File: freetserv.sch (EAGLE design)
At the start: 63 parts, among them IC2 SN75240PW, Q1 12MHz, Q2 6MHz, U1 MCP16311-E/MS, U4 TLV810SDBZT, U5 SN74LVC1G86DCKR

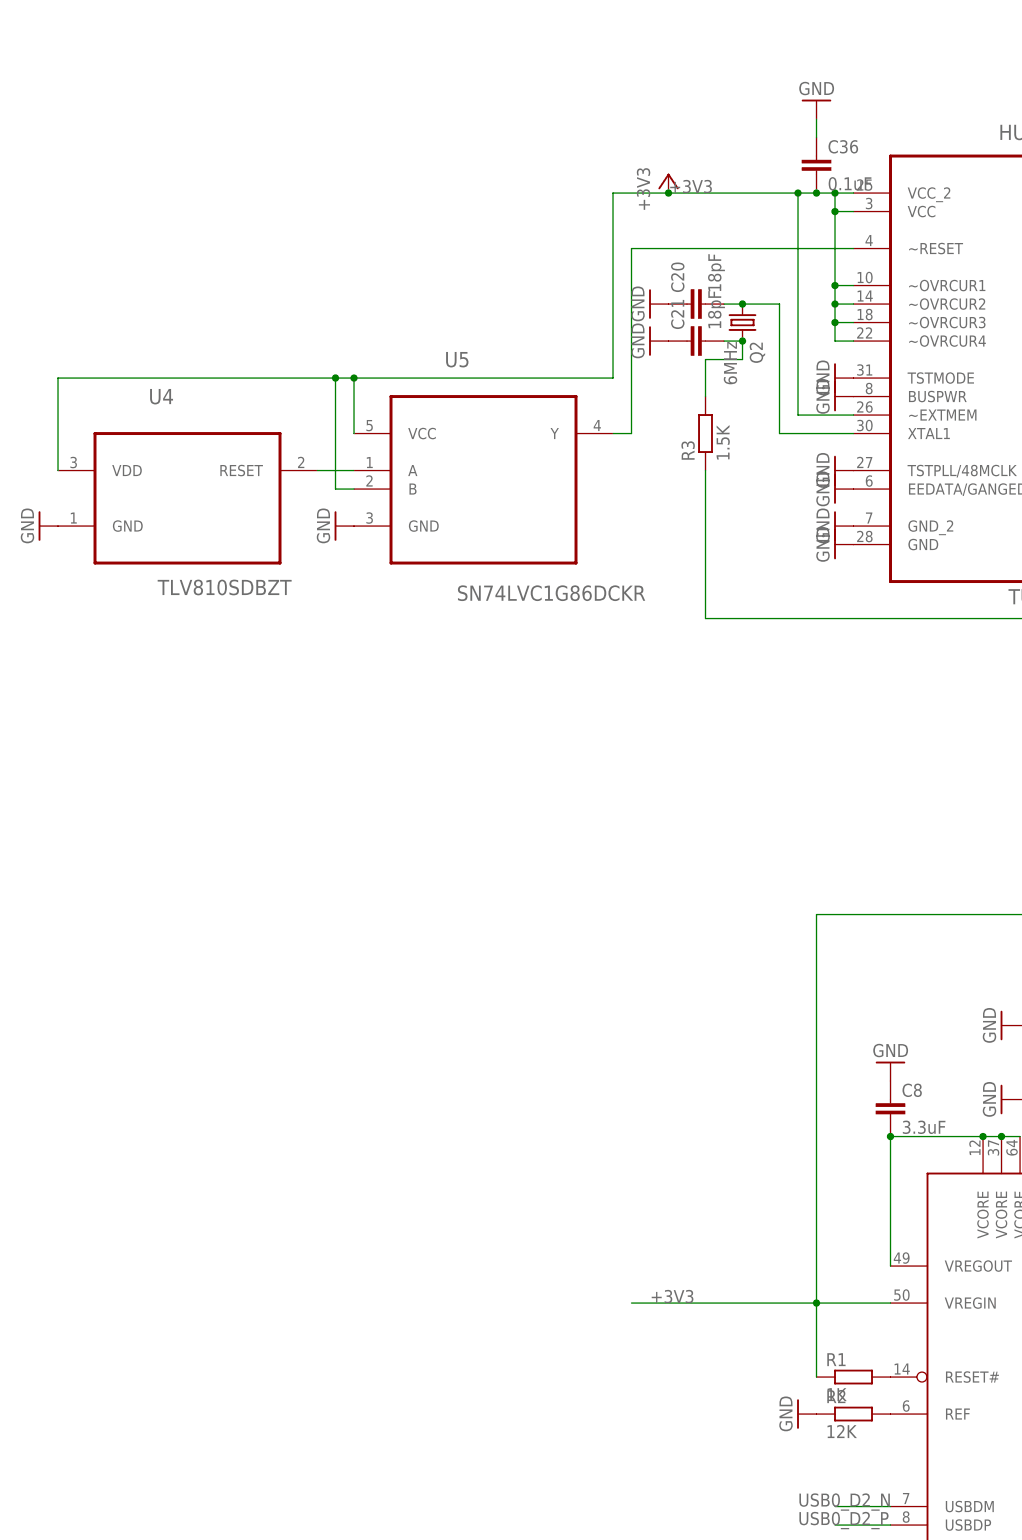
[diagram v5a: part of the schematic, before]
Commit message: replace volt supervisor IC with R/C circuit
Not yet routed to the FTDI, because that area still needs some
re-routing anyway.

fixes #5
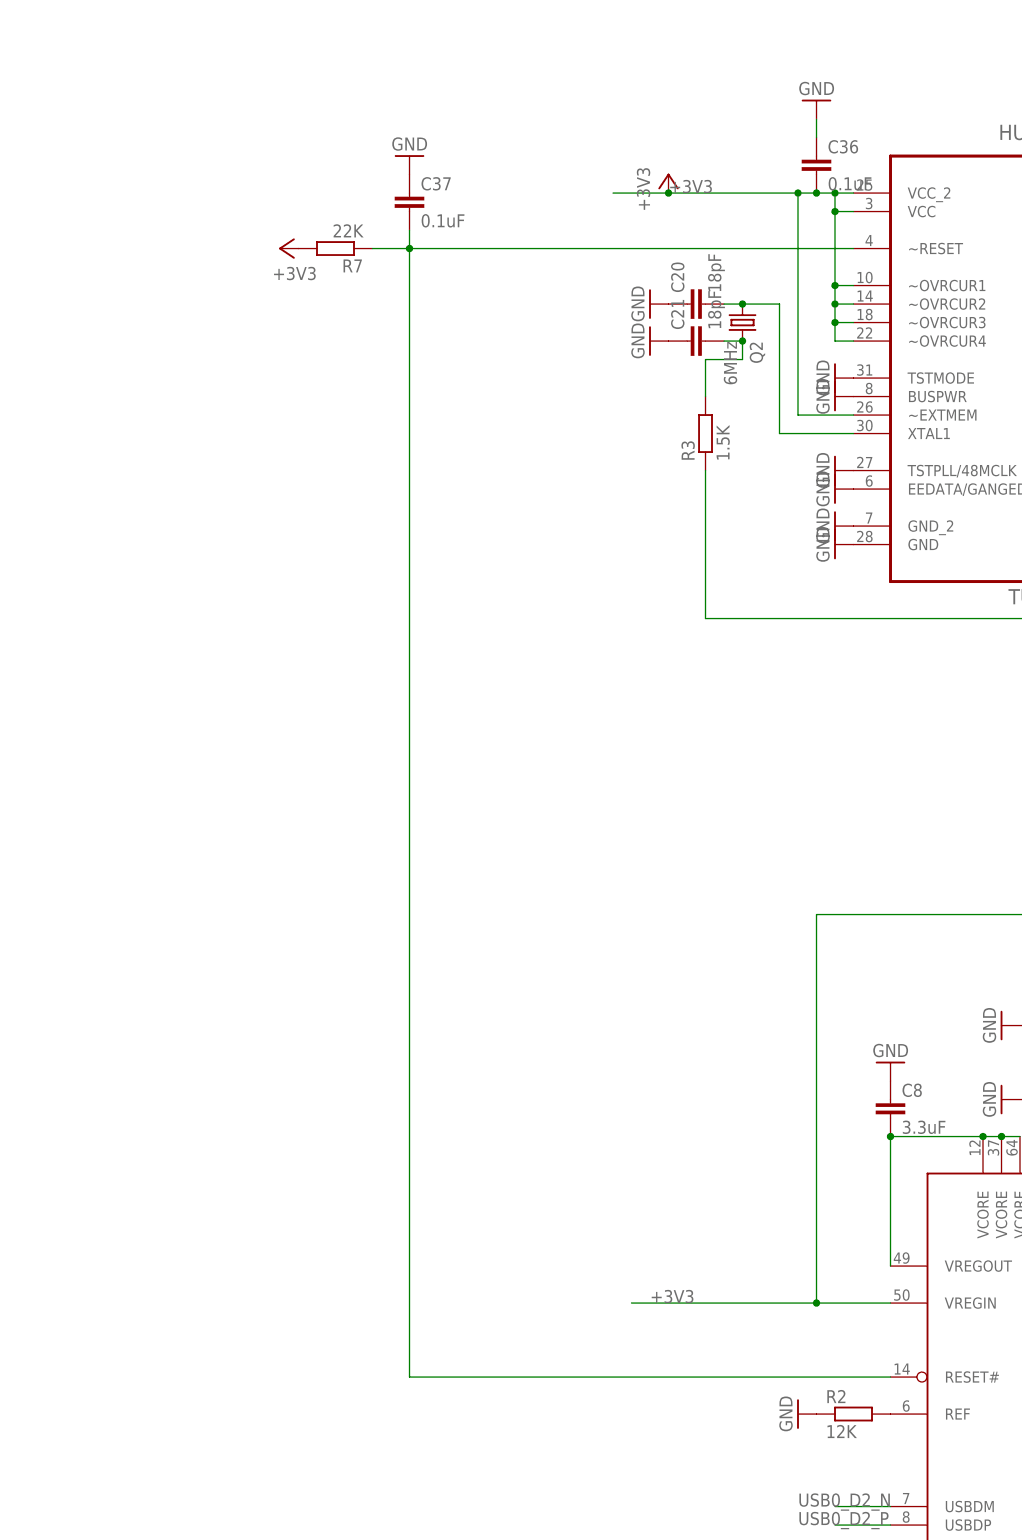
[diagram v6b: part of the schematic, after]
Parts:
- removed R1: 1K, resistor:R-EU_R0805
- removed U4: TLV810SDBZT, Texas Instruments_By_element14_Batch_1:TLV810SDBZT
- removed U5: SN74LVC1G86DCKR, Texas Instruments_By_element14_Batch_1:SN74LVC1G86DCKR
- added C37: 0.1uF, resistor:C-EUC0805
- added R7: 22K, resistor:R-EU_R0805
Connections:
- removed net N$13: R1.2, SERIAL0CORE.RESET#
- removed net N$42: U4.RESET, U5.A
- net +3V3: now also R7.2; no longer R1.1, U4.VDD, U5.B, U5.VCC
- net GND: now also C37.1; no longer U4.GND, U5.GND
- net N$43: now also C37.2, R7.1, SERIAL0CORE.RESET#; no longer U5.Y
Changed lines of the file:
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@@
 </part>
 <part name="GND14" library="supply1" deviceset="GND" device=""/>
-<part name="R1" library="resistor" deviceset="R-EU_" device="R0805" value="1K">
-<attribute name="PARTNO" value="311-1.0KARCT-ND"/>
-</part>
 <part name="R2" library="resistor" deviceset="R-EU_" device="R0805" value="12K">
 <attribute name="PARTNO" value="311-12.0KCRCT-ND"/>
@@
 <part name="GND23" library="supply1" deviceset="GND" device=""/>
 <part name="GND24" library="supply1" deviceset="GND" device=""/>
-<part name="U4" library="Texas Instruments_By_element14_Batch_1" deviceset="TLV810SDBZT" device=""/>
 <part name="DRIVER0A" library="Texas Instruments_By_element14_Batch_1" deviceset="MAX3232CPWR" device="">
 <attribute name="PARTNO" value="296-19263-1-ND"/>
@@
 <part name="GND28" library="supply1" deviceset="GND" device=""/>
 <part name="GND29" library="supply1" deviceset="GND" device=""/>
-<part name="GND30" library="supply1" deviceset="GND" device=""/>
 <part name="C19" library="resistor" deviceset="C-EU" device="C0805" value="0.1uF">
 <attribute name="PARTNO" value="1276-1003-1-ND"/>
 </part>
 <part name="GND31" library="supply1" deviceset="GND" device=""/>
-<part name="U5" library="Texas Instruments_By_element14_Batch_1" deviceset="SN74LVC1G86DCKR" device=""/>
-<part name="GND32" library="supply1" deviceset="GND" device=""/>
 <part name="Q2" library="crystal" deviceset="CSM-7X-DU" device="" value="6MHz">
 <attribute name="PARTNO" value="535-10208-1-ND"/>
@@
 </part>
 <part name="P+2" library="supply1" deviceset="+3V3" device=""/>
+<part name="C37" library="resistor" deviceset="C-EU" device="C0805" value="0.1uF">
+<attribute name="PARTNO" value="1276-1003-1-ND"/>
+</part>
+<part name="R7" library="resistor" deviceset="R-EU_" device="R0805" value="22K">
+<attribute name="PARTNO" value="311-22KARCT-ND"/>
+</part>
+<part name="P+3" library="supply1" deviceset="+3V3" device=""/>
+<part name="GND30" library="supply1" deviceset="GND" device=""/>
 </parts>
 <sheets>
@@
 </instance>
 <instance part="GND14" gate="1" x="5.08" y="104.14" rot="R180"/>
-<instance part="R1" gate="G$1" x="0" y="60.96">
-<attribute name="PARTNO" x="0" y="60.96" size="1.778" layer="96" display="off"/>
-</instance>
 <instance part="R2" gate="G$1" x="0" y="55.88">
 <attribute name="PARTNO" x="0" y="55.88" size="1.778" layer="96" display="off"/>
@@
 <instance part="GND23" gate="1" x="45.72" y="109.22" rot="R90"/>
 <instance part="GND24" gate="1" x="45.72" y="99.06" rot="R90"/>
-<instance part="U4" gate="A" x="-91.44" y="185.42"/>
 <instance part="DRIVER0A" gate="A" x="160.02" y="99.06">
 <attribute name="PARTNO" x="160.02" y="99.06" size="1.778" layer="96" display="off"/>
@@
 <instance part="GND28" gate="1" x="132.08" y="78.74" rot="R270"/>
 <instance part="GND29" gate="1" x="132.08" y="114.3" rot="R270"/>
-<instance part="GND30" gate="1" x="-111.76" y="177.8" rot="R270"/>
 <instance part="C19" gate="G$1" x="127" y="111.76" rot="R180">
 <attribute name="PARTNO" x="127" y="111.76" size="1.778" layer="96" display="off"/>
 </instance>
 <instance part="GND31" gate="1" x="127" y="106.68"/>
-<instance part="U5" gate="A" x="-50.8" y="187.96"/>
-<instance part="GND32" gate="1" x="-71.12" y="177.8" rot="R270"/>
 <instance part="Q2" gate="P" x="-15.24" y="205.74" rot="R270">
 <attribute name="PARTNO" x="-15.24" y="205.74" size="1.778" layer="96" display="off"/>
@@
 </instance>
 <instance part="P+2" gate="G$1" x="-25.4" y="226.06"/>
+<instance part="C37" gate="G$1" x="-60.96" y="223.52">
+<attribute name="PARTNO" x="-60.96" y="223.52" size="1.778" layer="96" display="off"/>
+</instance>
+<instance part="R7" gate="G$1" x="-71.12" y="215.9" rot="R180">
+<attribute name="PARTNO" x="-71.12" y="215.9" size="1.778" layer="96" rot="R90" display="off"/>
+</instance>
+<instance part="P+3" gate="G$1" x="-78.74" y="215.9" rot="R90"/>
+<instance part="GND30" gate="1" x="-60.96" y="228.6" rot="R180"/>
 </instances>
 <busses>
@@
 </segment>
 <segment>
-<pinref part="U4" gate="A" pin="GND"/>
-<pinref part="GND30" gate="1" pin="GND"/>
-</segment>
-<segment>
 <pinref part="C19" gate="G$1" pin="1"/>
 <pinref part="GND31" gate="1" pin="GND"/>
-</segment>
-<segment>
-<pinref part="U5" gate="A" pin="GND"/>
-<pinref part="GND32" gate="1" pin="GND"/>
 </segment>
 <segment>
@@
 <pinref part="GND49" gate="1" pin="GND"/>
 </segment>
+<segment>
+<pinref part="C37" gate="G$1" pin="1"/>
+<pinref part="GND30" gate="1" pin="GND"/>
+</segment>
 </net>
 <net name="USB0_DM_P" class="0">
@@
 </segment>
 </net>
-<net name="N$13" class="0">
-<segment>
-<pinref part="SERIAL0" gate="CORE" pin="RESET#"/>
-<pinref part="R1" gate="G$1" pin="2"/>
-</segment>
-</net>
 <net name="N$14" class="0">
 <segment>
@@
 </segment>
 </net>
-<net name="N$42" class="0">
-<segment>
-<pinref part="U4" gate="A" pin="RESET"/>
-<pinref part="U5" gate="A" pin="A"/>
-<wire x1="-73.66" y1="185.42" x2="-68.58" y2="185.42" width="0.1524" layer="91"/>
-</segment>
-</net>
 <net name="N$43" class="0">
 <segment>
 <pinref part="HUB0" gate="A" pin="~RESET"/>
-<wire x1="0" y1="215.9" x2="-30.48" y2="215.9" width="0.1524" layer="91"/>
-<pinref part="U5" gate="A" pin="Y"/>
-<wire x1="-30.48" y1="190.5" x2="-33.02" y2="190.5" width="0.1524" layer="91"/>
-<wire x1="-30.48" y1="215.9" x2="-30.48" y2="190.5" width="0.1524" layer="91"/>
+<pinref part="R7" gate="G$1" pin="1"/>
+<wire x1="-66.04" y1="215.9" x2="-60.96" y2="215.9" width="0.1524" layer="91"/>
+<pinref part="C37" gate="G$1" pin="2"/>
+<wire x1="-60.96" y1="215.9" x2="0" y2="215.9" width="0.1524" layer="91"/>
+<wire x1="-60.96" y1="218.44" x2="-60.96" y2="215.9" width="0.1524" layer="91"/>
+<junction x="-60.96" y="215.9"/>
+<pinref part="SERIAL0" gate="CORE" pin="RESET#"/>
+<wire x1="5.08" y1="60.96" x2="-60.96" y2="60.96" width="0.1524" layer="91"/>
+<wire x1="-60.96" y1="60.96" x2="-60.96" y2="215.9" width="0.1524" layer="91"/>
 </segment>
 </net>
@@
 <net name="+3V3" class="2">
 <segment>
-<pinref part="U4" gate="A" pin="VDD"/>
-<wire x1="-109.22" y1="185.42" x2="-109.22" y2="198.12" width="0.1524" layer="91"/>
-<wire x1="-109.22" y1="198.12" x2="-71.12" y2="198.12" width="0.1524" layer="91"/>
-<wire x1="-71.12" y1="198.12" x2="-68.58" y2="198.12" width="0.1524" layer="91"/>
-<wire x1="-68.58" y1="198.12" x2="-33.02" y2="198.12" width="0.1524" layer="91"/>
-<pinref part="U5" gate="A" pin="VCC"/>
-<wire x1="-68.58" y1="190.5" x2="-68.58" y2="198.12" width="0.1524" layer="91"/>
-<junction x="-68.58" y="198.12"/>
-<pinref part="U5" gate="A" pin="B"/>
-<wire x1="-68.58" y1="182.88" x2="-71.12" y2="182.88" width="0.1524" layer="91"/>
-<wire x1="-71.12" y1="182.88" x2="-71.12" y2="198.12" width="0.1524" layer="91"/>
-<junction x="-71.12" y="198.12"/>
 <pinref part="HUB0" gate="A" pin="VCC_2"/>
 <wire x1="-7.62" y1="223.52" x2="-5.08" y2="223.52" width="0.1524" layer="91"/>
@@
 <label x="-25.4" y="223.52" size="1.778" layer="95"/>
 <wire x1="-25.4" y1="223.52" x2="-7.62" y2="223.52" width="0.1524" layer="91"/>
-<wire x1="-33.02" y1="223.52" x2="-33.02" y2="198.12" width="0.1524" layer="91"/>
 <pinref part="C36" gate="G$1" pin="2"/>
 <junction x="-5.08" y="223.52"/>
@@
 <pinref part="SERIAL0" gate="CORE" pin="VREGIN"/>
 <wire x1="-30.48" y1="71.12" x2="-5.08" y2="71.12" width="0.1524" layer="91"/>
-<pinref part="R1" gate="G$1" pin="1"/>
 <wire x1="-5.08" y1="71.12" x2="5.08" y2="71.12" width="0.1524" layer="91"/>
-<wire x1="-5.08" y1="60.96" x2="-5.08" y2="71.12" width="0.1524" layer="91"/>
 <junction x="-5.08" y="71.12"/>
 <wire x1="-5.08" y1="71.12" x2="-5.08" y2="124.46" width="0.1524" layer="91"/>
@@
 <label x="81.28" y="332.74" size="1.778" layer="95"/>
 </segment>
-</net>
+<segment>
+<pinref part="R7" gate="G$1" pin="2"/>
+<pinref part="P+3" gate="G$1" pin="+3V3"/>
+</segment>
+</net>
